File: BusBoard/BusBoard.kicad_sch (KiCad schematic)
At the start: 45 parts, among them J1 Conn_L10, J10 Conn_L1, J11 Conn_R1, J12 Conn_R2, J13 Conn_R3, J14 Conn_R4, J15 Conn_R5, J16 Conn_R6, J17 Conn_R7, J18 Conn_R8, J19 Conn_R9, J2 Conn_L9, J20 Conn_R10, J21 From Supply, J22 To Busboard, J3 Conn_L8, J4 Conn_L7, J5 Conn_L6, J6 Conn_L5, J7 Conn_L4, J8 Conn_L3, J9 Conn_L2

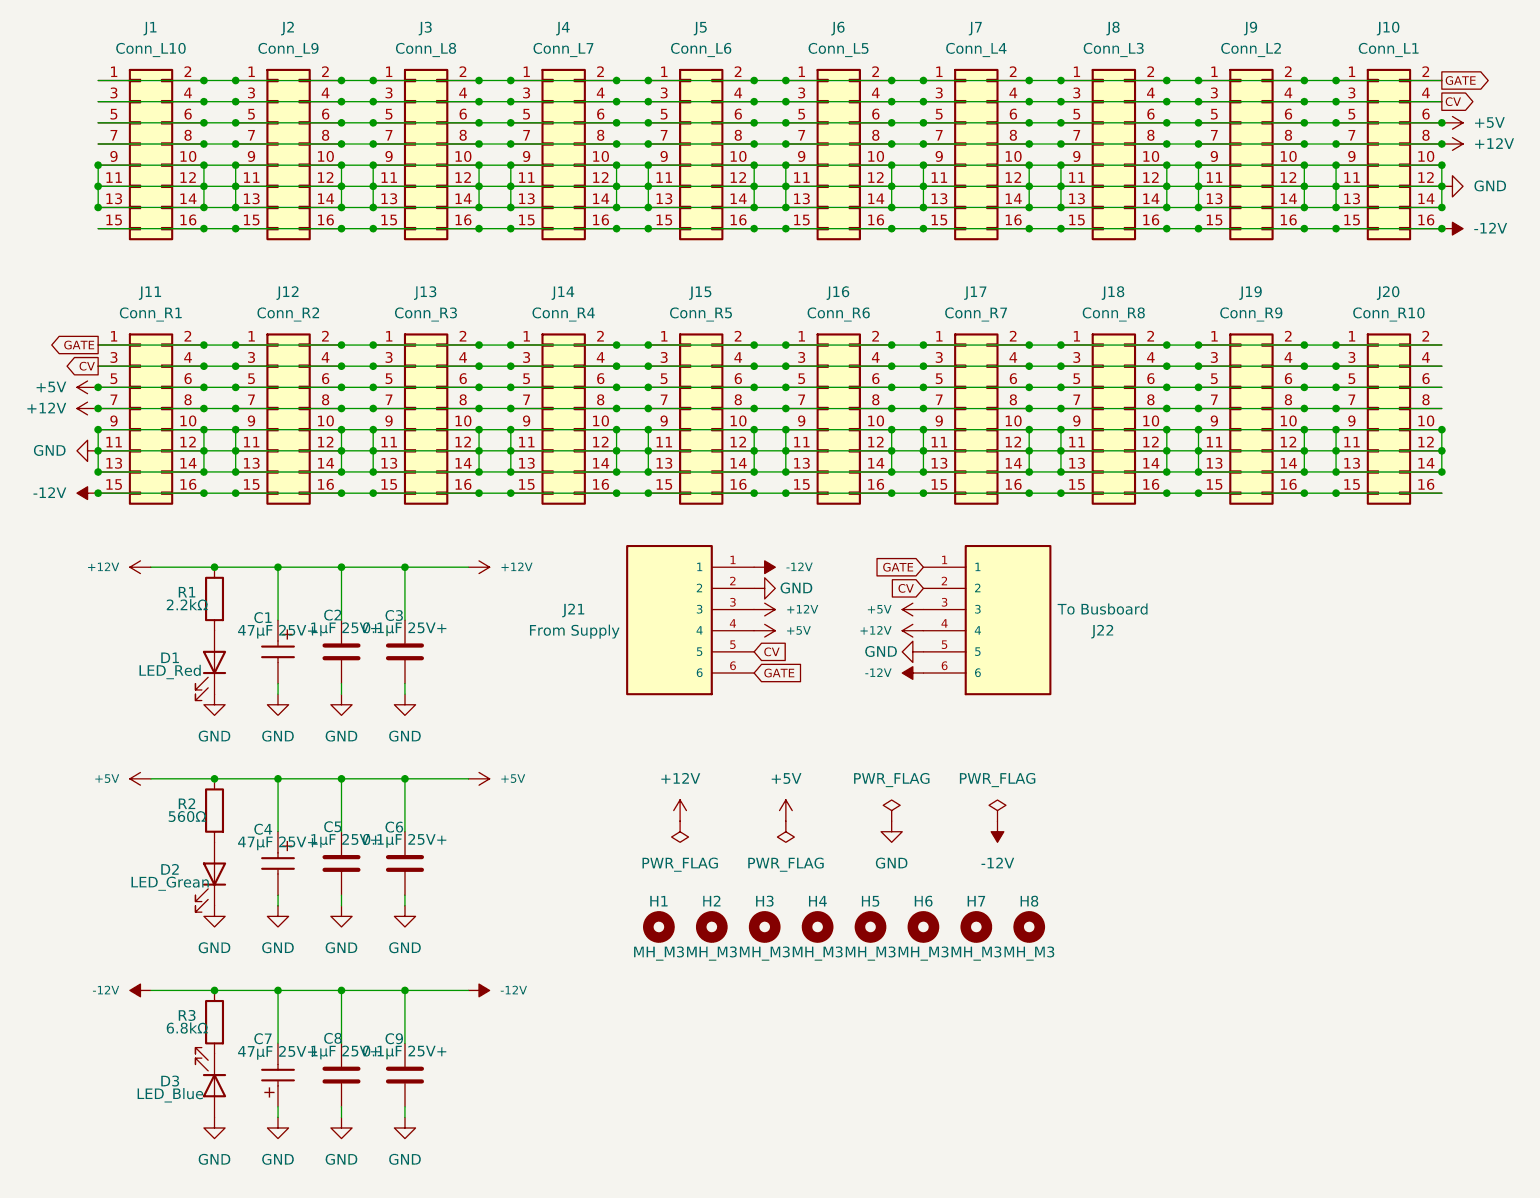
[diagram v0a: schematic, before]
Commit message: fix 16pin layout
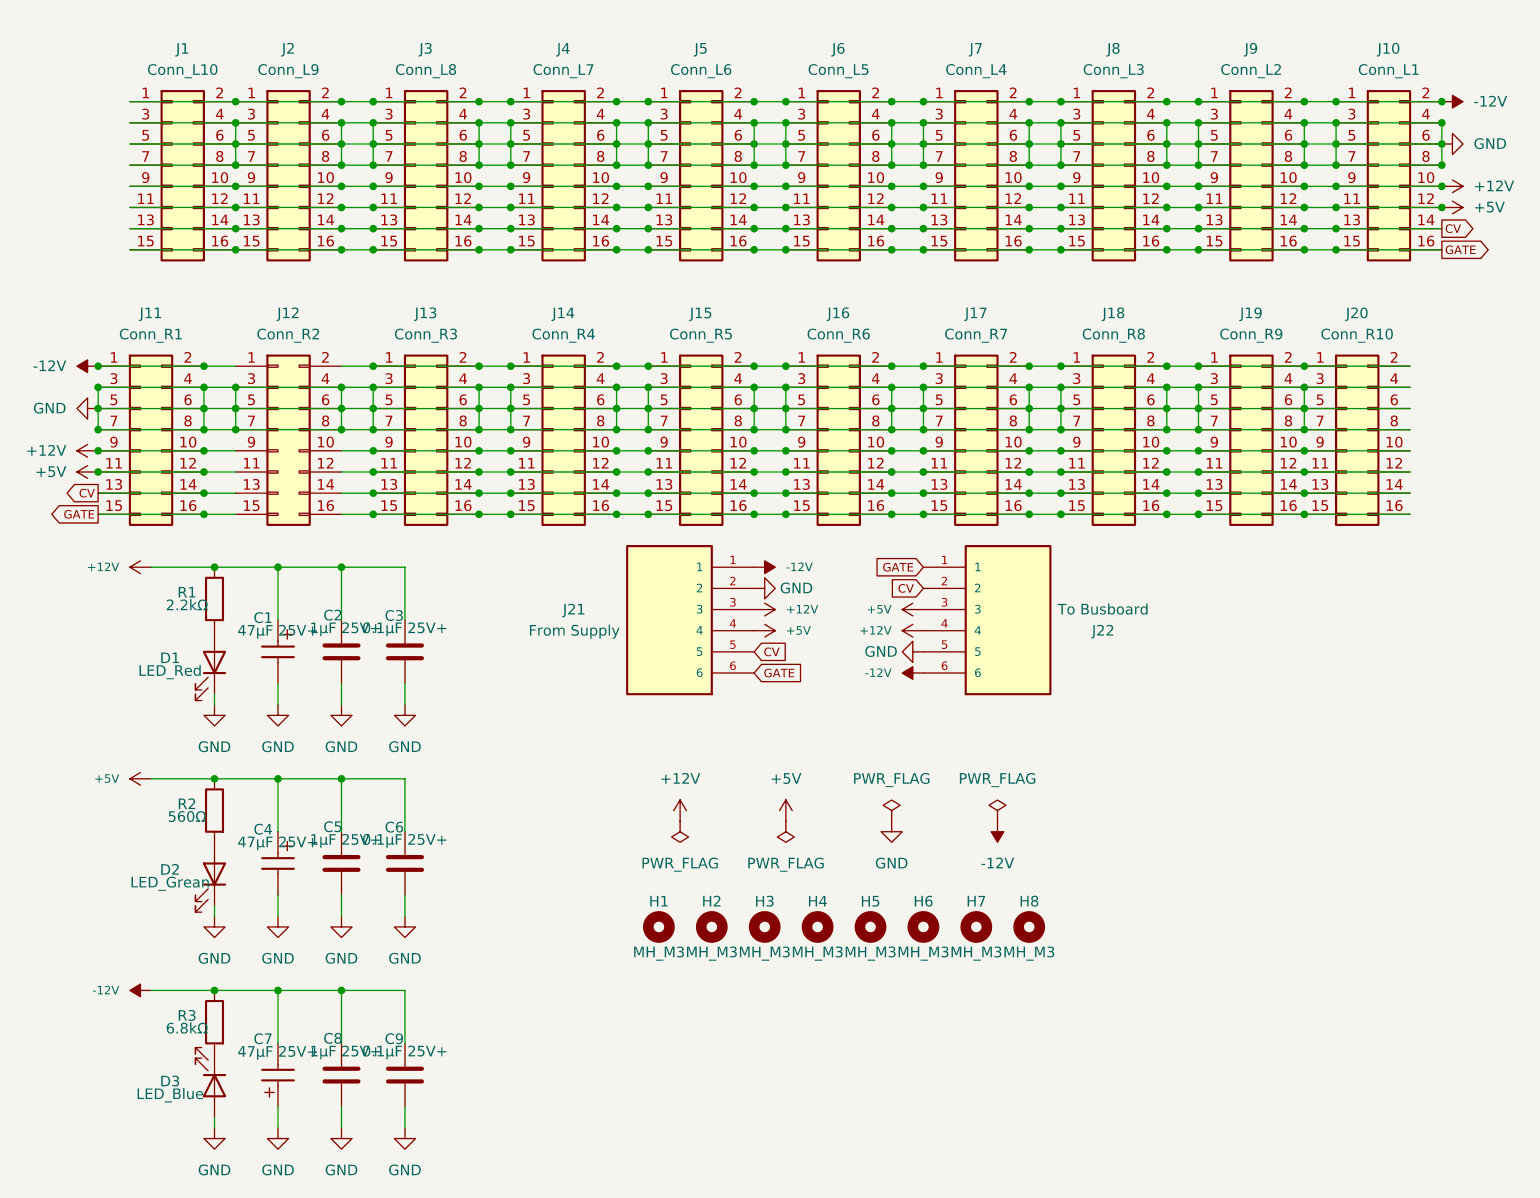
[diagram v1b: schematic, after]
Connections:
- net +12V: now also J1.10 (Pin_10), J1.9 (Pin_9), J10.10 (Pin_10), J10.9 (Pin_9), J11.10 (Pin_10), J11.9 (Pin_9), J12.9 (Pin_9), J2.10 (Pin_10), J2.9 (Pin_9), J3.10 (Pin_10), J3.9 (Pin_9), J4.10 (Pin_10), J4.9 (Pin_9), J5.10 (Pin_10), J5.9 (Pin_9), J6.10 (Pin_10), J6.9 (Pin_9), J7.10 (Pin_10), J7.9 (Pin_9), J8.10 (Pin_10), J8.9 (Pin_9), J9.10 (Pin_10), J9.9 (Pin_9); no longer J1.7 (Pin_7), J1.8 (Pin_8), J10.7 (Pin_7), J10.8 (Pin_8), J11.7 (Pin_7), J11.8 (Pin_8), J12.7 (Pin_7), J12.8 (Pin_8), J13.7 (Pin_7), J13.8 (Pin_8), J14.7 (Pin_7), J14.8 (Pin_8), J15.7 (Pin_7), J15.8 (Pin_8), J16.7 (Pin_7), J16.8 (Pin_8), J17.7 (Pin_7), J17.8 (Pin_8), J18.7 (Pin_7), J18.8 (Pin_8), J19.7 (Pin_7), J19.8 (Pin_8), J2.7 (Pin_7), J2.8 (Pin_8), J20.7 (Pin_7), J20.8 (Pin_8), J3.7 (Pin_7), J3.8 (Pin_8), J4.7 (Pin_7), J4.8 (Pin_8), J5.7 (Pin_7), J5.8 (Pin_8), J6.7 (Pin_7), J6.8 (Pin_8), J7.7 (Pin_7), J7.8 (Pin_8), J8.7 (Pin_7), J8.8 (Pin_8), J9.7 (Pin_7), J9.8 (Pin_8)
- net +5V: now also J1.11 (Pin_11), J1.12 (Pin_12), J10.11 (Pin_11), J10.12 (Pin_12), J11.11 (Pin_11), J11.12 (Pin_12), J12.11 (Pin_11), J2.11 (Pin_11), J2.12 (Pin_12), J3.11 (Pin_11), J3.12 (Pin_12), J4.11 (Pin_11), J4.12 (Pin_12), J5.11 (Pin_11), J5.12 (Pin_12), J6.11 (Pin_11), J6.12 (Pin_12), J7.11 (Pin_11), J7.12 (Pin_12), J8.11 (Pin_11), J8.12 (Pin_12), J9.11 (Pin_11), J9.12 (Pin_12); no longer J1.5 (Pin_5), J1.6 (Pin_6), J10.5 (Pin_5), J10.6 (Pin_6), J11.5 (Pin_5), J11.6 (Pin_6), J12.5 (Pin_5), J12.6 (Pin_6), J13.5 (Pin_5), J13.6 (Pin_6), J14.5 (Pin_5), J14.6 (Pin_6), J15.5 (Pin_5), J15.6 (Pin_6), J16.5 (Pin_5), J16.6 (Pin_6), J17.5 (Pin_5), J17.6 (Pin_6), J18.5 (Pin_5), J18.6 (Pin_6), J19.5 (Pin_5), J19.6 (Pin_6), J2.5 (Pin_5), J2.6 (Pin_6), J20.5 (Pin_5), J20.6 (Pin_6), J3.5 (Pin_5), J3.6 (Pin_6), J4.5 (Pin_5), J4.6 (Pin_6), J5.5 (Pin_5), J5.6 (Pin_6), J6.5 (Pin_5), J6.6 (Pin_6), J7.5 (Pin_5), J7.6 (Pin_6), J8.5 (Pin_5), J8.6 (Pin_6), J9.5 (Pin_5), J9.6 (Pin_6)
- net -12V: now also J1.1 (Pin_1), J1.2 (Pin_2), J10.1 (Pin_1), J10.2 (Pin_2), J11.1 (Pin_1), J11.2 (Pin_2), J12.1 (Pin_1), J2.1 (Pin_1), J2.2 (Pin_2), J3.1 (Pin_1), J3.2 (Pin_2), J4.1 (Pin_1), J4.2 (Pin_2), J5.1 (Pin_1), J5.2 (Pin_2), J6.1 (Pin_1), J6.2 (Pin_2), J7.1 (Pin_1), J7.2 (Pin_2), J8.1 (Pin_1), J8.2 (Pin_2), J9.1 (Pin_1), J9.2 (Pin_2); no longer J1.15 (Pin_15), J1.16 (Pin_16), J10.15 (Pin_15), J10.16 (Pin_16), J11.15 (Pin_15), J11.16 (Pin_16), J12.15 (Pin_15), J12.16 (Pin_16), J13.15 (Pin_15), J13.16 (Pin_16), J14.15 (Pin_15), J14.16 (Pin_16), J15.15 (Pin_15), J15.16 (Pin_16), J16.15 (Pin_15), J16.16 (Pin_16), J17.15 (Pin_15), J17.16 (Pin_16), J18.15 (Pin_15), J18.16 (Pin_16), J19.15 (Pin_15), J19.16 (Pin_16), J2.15 (Pin_15), J2.16 (Pin_16), J20.15 (Pin_15), J20.16 (Pin_16), J3.15 (Pin_15), J3.16 (Pin_16), J4.15 (Pin_15), J4.16 (Pin_16), J5.15 (Pin_15), J5.16 (Pin_16), J6.15 (Pin_15), J6.16 (Pin_16), J7.15 (Pin_15), J7.16 (Pin_16), J8.15 (Pin_15), J8.16 (Pin_16), J9.15 (Pin_15), J9.16 (Pin_16)
- net CV: now also J1.13 (Pin_13), J1.14 (Pin_14), J10.13 (Pin_13), J10.14 (Pin_14), J11.13 (Pin_13), J11.14 (Pin_14), J12.13 (Pin_13), J2.13 (Pin_13), J2.14 (Pin_14), J3.13 (Pin_13), J3.14 (Pin_14), J4.13 (Pin_13), J4.14 (Pin_14), J5.13 (Pin_13), J5.14 (Pin_14), J6.13 (Pin_13), J6.14 (Pin_14), J7.13 (Pin_13), J7.14 (Pin_14), J8.13 (Pin_13), J8.14 (Pin_14), J9.13 (Pin_13), J9.14 (Pin_14); no longer J1.3 (Pin_3), J1.4 (Pin_4), J10.3 (Pin_3), J10.4 (Pin_4), J11.3 (Pin_3), J11.4 (Pin_4), J12.3 (Pin_3), J12.4 (Pin_4), J13.3 (Pin_3), J13.4 (Pin_4), J14.3 (Pin_3), J14.4 (Pin_4), J15.3 (Pin_3), J15.4 (Pin_4), J16.3 (Pin_3), J16.4 (Pin_4), J17.3 (Pin_3), J17.4 (Pin_4), J18.3 (Pin_3), J18.4 (Pin_4), J19.3 (Pin_3), J19.4 (Pin_4), J2.3 (Pin_3), J2.4 (Pin_4), J20.3 (Pin_3), J20.4 (Pin_4), J3.3 (Pin_3), J3.4 (Pin_4), J4.3 (Pin_3), J4.4 (Pin_4), J5.3 (Pin_3), J5.4 (Pin_4), J6.3 (Pin_3), J6.4 (Pin_4), J7.3 (Pin_3), J7.4 (Pin_4), J8.3 (Pin_3), J8.4 (Pin_4), J9.3 (Pin_3), J9.4 (Pin_4)
- net GATE: now also J1.15 (Pin_15), J1.16 (Pin_16), J10.15 (Pin_15), J10.16 (Pin_16), J11.15 (Pin_15), J11.16 (Pin_16), J12.15 (Pin_15), J2.15 (Pin_15), J2.16 (Pin_16), J3.15 (Pin_15), J3.16 (Pin_16), J4.15 (Pin_15), J4.16 (Pin_16), J5.15 (Pin_15), J5.16 (Pin_16), J6.15 (Pin_15), J6.16 (Pin_16), J7.15 (Pin_15), J7.16 (Pin_16), J8.15 (Pin_15), J8.16 (Pin_16), J9.15 (Pin_15), J9.16 (Pin_16); no longer J1.1 (Pin_1), J1.2 (Pin_2), J10.1 (Pin_1), J10.2 (Pin_2), J11.1 (Pin_1), J11.2 (Pin_2), J12.1 (Pin_1), J12.2 (Pin_2), J13.1 (Pin_1), J13.2 (Pin_2), J14.1 (Pin_1), J14.2 (Pin_2), J15.1 (Pin_1), J15.2 (Pin_2), J16.1 (Pin_1), J16.2 (Pin_2), J17.1 (Pin_1), J17.2 (Pin_2), J18.1 (Pin_1), J18.2 (Pin_2), J19.1 (Pin_1), J19.2 (Pin_2), J2.1 (Pin_1), J2.2 (Pin_2), J20.1 (Pin_1), J20.2 (Pin_2), J3.1 (Pin_1), J3.2 (Pin_2), J4.1 (Pin_1), J4.2 (Pin_2), J5.1 (Pin_1), J5.2 (Pin_2), J6.1 (Pin_1), J6.2 (Pin_2), J7.1 (Pin_1), J7.2 (Pin_2), J8.1 (Pin_1), J8.2 (Pin_2), J9.1 (Pin_1), J9.2 (Pin_2)
- net GND: now also J1.3 (Pin_3), J1.4 (Pin_4), J1.5 (Pin_5), J1.6 (Pin_6), J1.7 (Pin_7), J1.8 (Pin_8), J10.3 (Pin_3), J10.4 (Pin_4), J10.5 (Pin_5), J10.6 (Pin_6), J10.7 (Pin_7), J10.8 (Pin_8), J11.3 (Pin_3), J11.4 (Pin_4), J11.5 (Pin_5), J11.6 (Pin_6), J11.7 (Pin_7), J11.8 (Pin_8), J12.3 (Pin_3), J12.4 (Pin_4), J12.5 (Pin_5), J12.6 (Pin_6), J12.7 (Pin_7), J12.8 (Pin_8), J13.3 (Pin_3), J13.4 (Pin_4), J13.5 (Pin_5), J13.6 (Pin_6), J13.7 (Pin_7), J13.8 (Pin_8), J14.3 (Pin_3), J14.4 (Pin_4), J14.5 (Pin_5), J14.6 (Pin_6), J14.7 (Pin_7), J14.8 (Pin_8), J15.3 (Pin_3), J15.4 (Pin_4), J15.5 (Pin_5), J15.6 (Pin_6), J15.7 (Pin_7), J15.8 (Pin_8), J16.3 (Pin_3), J16.4 (Pin_4), J16.5 (Pin_5), J16.6 (Pin_6), J16.7 (Pin_7), J16.8 (Pin_8), J17.3 (Pin_3), J17.4 (Pin_4), J17.5 (Pin_5), J17.6 (Pin_6), J17.7 (Pin_7), J17.8 (Pin_8), J18.3 (Pin_3), J18.4 (Pin_4), J18.5 (Pin_5), J18.6 (Pin_6), J18.7 (Pin_7), J18.8 (Pin_8), J19.3 (Pin_3), J19.4 (Pin_4), J19.5 (Pin_5), J19.6 (Pin_6), J19.7 (Pin_7), J19.8 (Pin_8), J2.3 (Pin_3), J2.4 (Pin_4), J2.5 (Pin_5), J2.6 (Pin_6), J2.7 (Pin_7), J2.8 (Pin_8), J20.3 (Pin_3), J20.4 (Pin_4), J20.5 (Pin_5), J20.6 (Pin_6), J20.7 (Pin_7), J20.8 (Pin_8), J3.3 (Pin_3), J3.4 (Pin_4), J3.5 (Pin_5), J3.6 (Pin_6), J3.7 (Pin_7), J3.8 (Pin_8), J4.3 (Pin_3), J4.4 (Pin_4), J4.5 (Pin_5), J4.6 (Pin_6), J4.7 (Pin_7), J4.8 (Pin_8), J5.3 (Pin_3), J5.4 (Pin_4), J5.5 (Pin_5), J5.6 (Pin_6), J5.7 (Pin_7), J5.8 (Pin_8), J6.3 (Pin_3), J6.4 (Pin_4), J6.5 (Pin_5), J6.6 (Pin_6), J6.7 (Pin_7), J6.8 (Pin_8), J7.3 (Pin_3), J7.4 (Pin_4), J7.5 (Pin_5), J7.6 (Pin_6), J7.7 (Pin_7), J7.8 (Pin_8), J8.3 (Pin_3), J8.4 (Pin_4), J8.5 (Pin_5), J8.6 (Pin_6), J8.7 (Pin_7), J8.8 (Pin_8), J9.3 (Pin_3), J9.4 (Pin_4), J9.5 (Pin_5), J9.6 (Pin_6), J9.7 (Pin_7), J9.8 (Pin_8); no longer J1.10 (Pin_10), J1.11 (Pin_11), J1.12 (Pin_12), J1.13 (Pin_13), J1.14 (Pin_14), J1.9 (Pin_9), J10.10 (Pin_10), J10.11 (Pin_11), J10.12 (Pin_12), J10.13 (Pin_13), J10.14 (Pin_14), J10.9 (Pin_9), J11.10 (Pin_10), J11.11 (Pin_11), J11.12 (Pin_12), J11.13 (Pin_13), J11.14 (Pin_14), J11.9 (Pin_9), J12.10 (Pin_10), J12.11 (Pin_11), J12.12 (Pin_12), J12.13 (Pin_13), J12.14 (Pin_14), J12.9 (Pin_9), J13.10 (Pin_10), J13.11 (Pin_11), J13.12 (Pin_12), J13.13 (Pin_13), J13.14 (Pin_14), J13.9 (Pin_9), J14.10 (Pin_10), J14.11 (Pin_11), J14.12 (Pin_12), J14.13 (Pin_13), J14.14 (Pin_14), J14.9 (Pin_9), J15.10 (Pin_10), J15.11 (Pin_11), J15.12 (Pin_12), J15.13 (Pin_13), J15.14 (Pin_14), J15.9 (Pin_9), J16.10 (Pin_10), J16.11 (Pin_11), J16.12 (Pin_12), J16.13 (Pin_13), J16.14 (Pin_14), J16.9 (Pin_9), J17.10 (Pin_10), J17.11 (Pin_11), J17.12 (Pin_12), J17.13 (Pin_13), J17.14 (Pin_14), J17.9 (Pin_9), J18.10 (Pin_10), J18.11 (Pin_11), J18.12 (Pin_12), J18.13 (Pin_13), J18.14 (Pin_14), J18.9 (Pin_9), J19.10 (Pin_10), J19.11 (Pin_11), J19.12 (Pin_12), J19.13 (Pin_13), J19.14 (Pin_14), J19.9 (Pin_9), J2.10 (Pin_10), J2.11 (Pin_11), J2.12 (Pin_12), J2.13 (Pin_13), J2.14 (Pin_14), J2.9 (Pin_9), J20.10 (Pin_10), J20.11 (Pin_11), J20.12 (Pin_12), J20.13 (Pin_13), J20.14 (Pin_14), J20.9 (Pin_9), J3.10 (Pin_10), J3.11 (Pin_11), J3.12 (Pin_12), J3.13 (Pin_13), J3.14 (Pin_14), J3.9 (Pin_9), J4.10 (Pin_10), J4.11 (Pin_11), J4.12 (Pin_12), J4.13 (Pin_13), J4.14 (Pin_14), J4.9 (Pin_9), J5.10 (Pin_10), J5.11 (Pin_11), J5.12 (Pin_12), J5.13 (Pin_13), J5.14 (Pin_14), J5.9 (Pin_9), J6.10 (Pin_10), J6.11 (Pin_11), J6.12 (Pin_12), J6.13 (Pin_13), J6.14 (Pin_14), J6.9 (Pin_9), J7.10 (Pin_10), J7.11 (Pin_11), J7.12 (Pin_12), J7.13 (Pin_13), J7.14 (Pin_14), J7.9 (Pin_9), J8.10 (Pin_10), J8.11 (Pin_11), J8.12 (Pin_12), J8.13 (Pin_13), J8.14 (Pin_14), J8.9 (Pin_9), J9.10 (Pin_10), J9.11 (Pin_11), J9.12 (Pin_12), J9.13 (Pin_13), J9.14 (Pin_14), J9.9 (Pin_9)
- new net: J12.2 (Pin_2), J13.1 (Pin_1), J13.2 (Pin_2), J14.1 (Pin_1), J14.2 (Pin_2), J15.1 (Pin_1), J15.2 (Pin_2), J16.1 (Pin_1), J16.2 (Pin_2), J17.1 (Pin_1), J17.2 (Pin_2), J18.1 (Pin_1), J18.2 (Pin_2), J19.1 (Pin_1), J19.2 (Pin_2), J20.1 (Pin_1), J20.2 (Pin_2)
- new net: J12.10 (Pin_10), J13.10 (Pin_10), J13.9 (Pin_9), J14.10 (Pin_10), J14.9 (Pin_9), J15.10 (Pin_10), J15.9 (Pin_9), J16.10 (Pin_10), J16.9 (Pin_9), J17.10 (Pin_10), J17.9 (Pin_9), J18.10 (Pin_10), J18.9 (Pin_9), J19.10 (Pin_10), J19.9 (Pin_9), J20.10 (Pin_10), J20.9 (Pin_9)
- new net: J12.12 (Pin_12), J13.11 (Pin_11), J13.12 (Pin_12), J14.11 (Pin_11), J14.12 (Pin_12), J15.11 (Pin_11), J15.12 (Pin_12), J16.11 (Pin_11), J16.12 (Pin_12), J17.11 (Pin_11), J17.12 (Pin_12), J18.11 (Pin_11), J18.12 (Pin_12), J19.11 (Pin_11), J19.12 (Pin_12), J20.11 (Pin_11), J20.12 (Pin_12)
- new net: J12.14 (Pin_14), J13.13 (Pin_13), J13.14 (Pin_14), J14.13 (Pin_13), J14.14 (Pin_14), J15.13 (Pin_13), J15.14 (Pin_14), J16.13 (Pin_13), J16.14 (Pin_14), J17.13 (Pin_13), J17.14 (Pin_14), J18.13 (Pin_13), J18.14 (Pin_14), J19.13 (Pin_13), J19.14 (Pin_14), J20.13 (Pin_13), J20.14 (Pin_14)
- new net: J12.16 (Pin_16), J13.15 (Pin_15), J13.16 (Pin_16), J14.15 (Pin_15), J14.16 (Pin_16), J15.15 (Pin_15), J15.16 (Pin_16), J16.15 (Pin_15), J16.16 (Pin_16), J17.15 (Pin_15), J17.16 (Pin_16), J18.15 (Pin_15), J18.16 (Pin_16), J19.15 (Pin_15), J19.16 (Pin_16), J20.15 (Pin_15), J20.16 (Pin_16)
